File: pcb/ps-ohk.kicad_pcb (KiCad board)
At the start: 2 copper layers, 27 parts

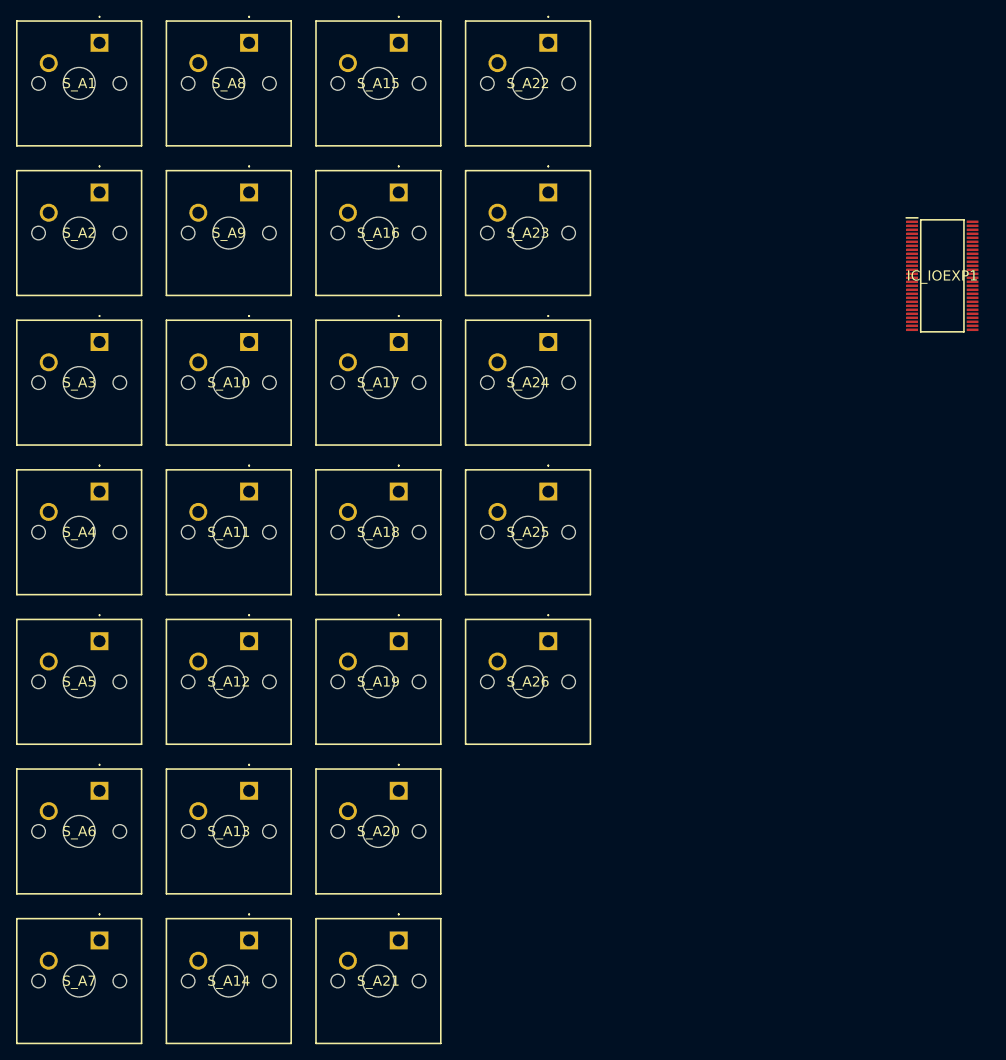
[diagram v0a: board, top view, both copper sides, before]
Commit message: pcb: implement IO Expander circuit based on proto
Signed-off-by: Dylan Turner <dylan.turner@tutanota.com>
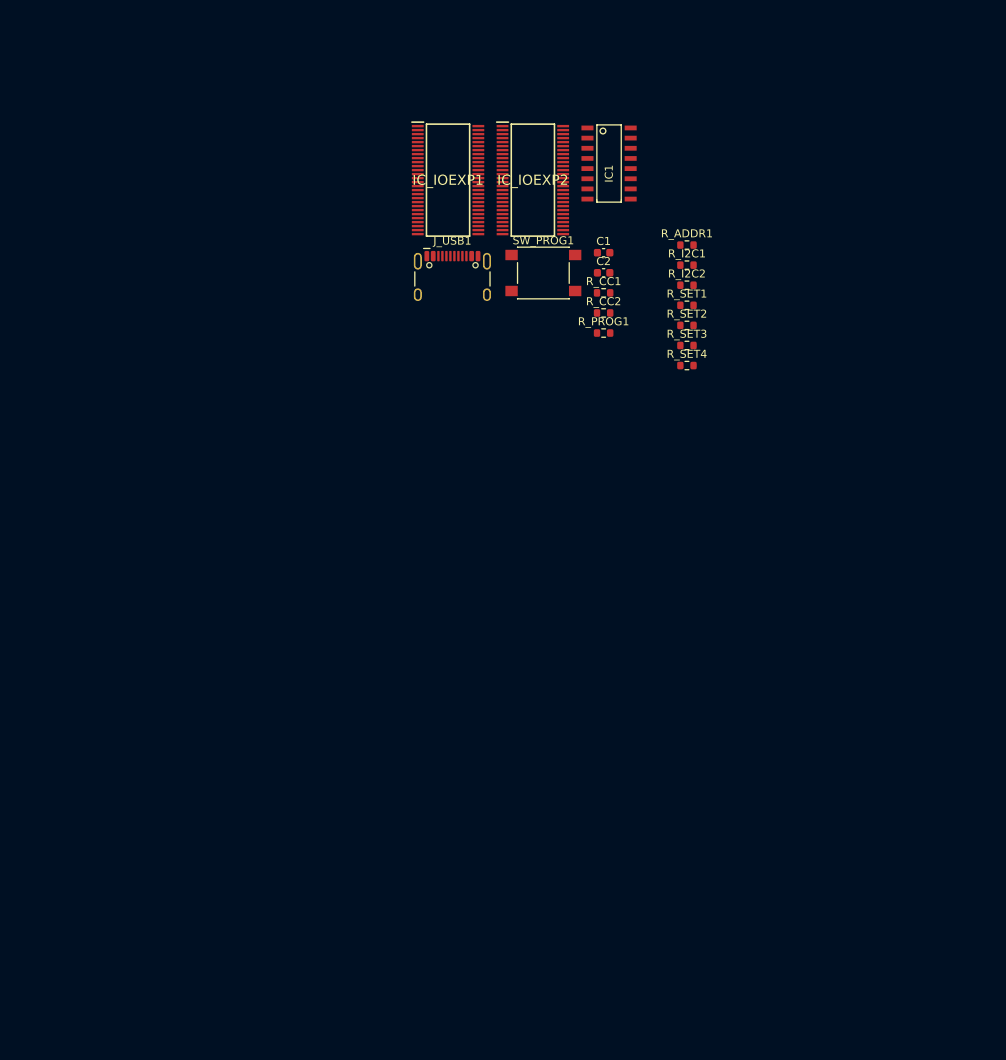
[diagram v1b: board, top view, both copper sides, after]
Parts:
- removed S_A1, S_A10, S_A11, S_A12, S_A13, S_A14, S_A15, S_A16, S_A17, S_A18, S_A19, S_A2, S_A20, S_A21, S_A22, S_A23, S_A24, S_A25, S_A26, S_A3, S_A4, S_A5, S_A6, S_A7, S_A8, S_A9: ~, COM-13834:COM13834
- added C1: 100nF, Capacitor_SMD:C_0603_1608Metric, F.Cu at (122.9, 78.9)
- added C2: 100nF, Capacitor_SMD:C_0603_1608Metric, F.Cu at (122.9, 81.4)
- added IC1: CH552G, ch552g:SOIC-16_3.9x9.9mm_Pitch1.27mm, F.Cu at (123.6, 67.7)
- added IC_IOEXP2: PCA9505DGGY, PCA9505DGGY:SOP50P810X120-56N, F.Cu at (114.0, 69.8)
- added J_USB1: ~, Connector_USB:USB_C_Receptacle_HCTL_HC-TYPE-C-16P-01A, F.Cu at (104.0, 83.0)
- added R_ADDR1: 1-10k, Resistor_SMD:R_0603_1608Metric, F.Cu at (133.3, 77.9)
- added R_CC1: 5.1k, Resistor_SMD:R_0603_1608Metric, F.Cu at (122.9, 83.9)
- added R_CC2: 5.1k, Resistor_SMD:R_0603_1608Metric, F.Cu at (122.9, 86.4)
- added R_I2C1: 1-10k, Resistor_SMD:R_0603_1608Metric, F.Cu at (133.3, 80.4)
- added R_I2C2: 1-10k, Resistor_SMD:R_0603_1608Metric, F.Cu at (133.3, 82.9)
- added R_PROG1: 10k, Resistor_SMD:R_0603_1608Metric, F.Cu at (122.9, 88.9)
- added R_SET1: 1-10k, Resistor_SMD:R_0603_1608Metric, F.Cu at (133.3, 85.4)
- added R_SET2: 1-10k, Resistor_SMD:R_0603_1608Metric, F.Cu at (133.3, 87.9)
- added R_SET3: 1-10k, Resistor_SMD:R_0603_1608Metric, F.Cu at (133.3, 90.5)
- added R_SET4: 1-10k, Resistor_SMD:R_0603_1608Metric, F.Cu at (133.3, 93.0)
- added SW_PROG1: ~, Button_Switch_SMD:SW_Push_1P1T_NO_6x6mm_H9.5mm, F.Cu at (115.3, 81.4)
- moved IC_IOEXP1 62.9 mm to (103.4, 69.8)
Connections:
- IC_IOEXP1 pad 1: unconnected-(IC_IOEXP1-SDA-Pad1) -> /SDA
- IC_IOEXP1 pad 11: unconnected-(IC_IOEXP1-VSS_2-Pad11) -> GND
- IC_IOEXP1 pad 18: unconnected-(IC_IOEXP1-VDD_1-Pad18) -> VCC
- IC_IOEXP1 pad 2: unconnected-(IC_IOEXP1-SCL-Pad2) -> /SCL
- IC_IOEXP1 pad 23: unconnected-(IC_IOEXP1-VSS_3-Pad23) -> GND
- IC_IOEXP1 pad 27: unconnected-(IC_IOEXP1-A0-Pad27) -> GND
- IC_IOEXP1 pad 28: unconnected-(IC_IOEXP1-A1-Pad28) -> GND
- IC_IOEXP1 pad 29: unconnected-(IC_IOEXP1-A2-Pad29) -> GND
- IC_IOEXP1 pad 3: unconnected-(IC_IOEXP1-IO0_0-Pad3) -> /KEY_A
- IC_IOEXP1 pad 30: unconnected-(IC_IOEXP1-~{OE}-Pad30) -> GND
- IC_IOEXP1 pad 34: unconnected-(IC_IOEXP1-VSS_4-Pad34) -> GND
- IC_IOEXP1 pad 39: unconnected-(IC_IOEXP1-VSS_5-Pad39) -> GND
- IC_IOEXP1 pad 46: unconnected-(IC_IOEXP1-VDD_2-Pad46) -> VCC
- IC_IOEXP1 pad 51: unconnected-(IC_IOEXP1-VSS_6-Pad51) -> GND
- IC_IOEXP1 pad 55: unconnected-(IC_IOEXP1-~{INT}-Pad55) -> Net-(IC_IOEXP1-~{INT})
- IC_IOEXP1 pad 56: unconnected-(IC_IOEXP1-~{RESET}-Pad56) -> Net-(IC_IOEXP1-~{RESET})
- IC_IOEXP1 pad 6: unconnected-(IC_IOEXP1-VSS_1-Pad6) -> GND

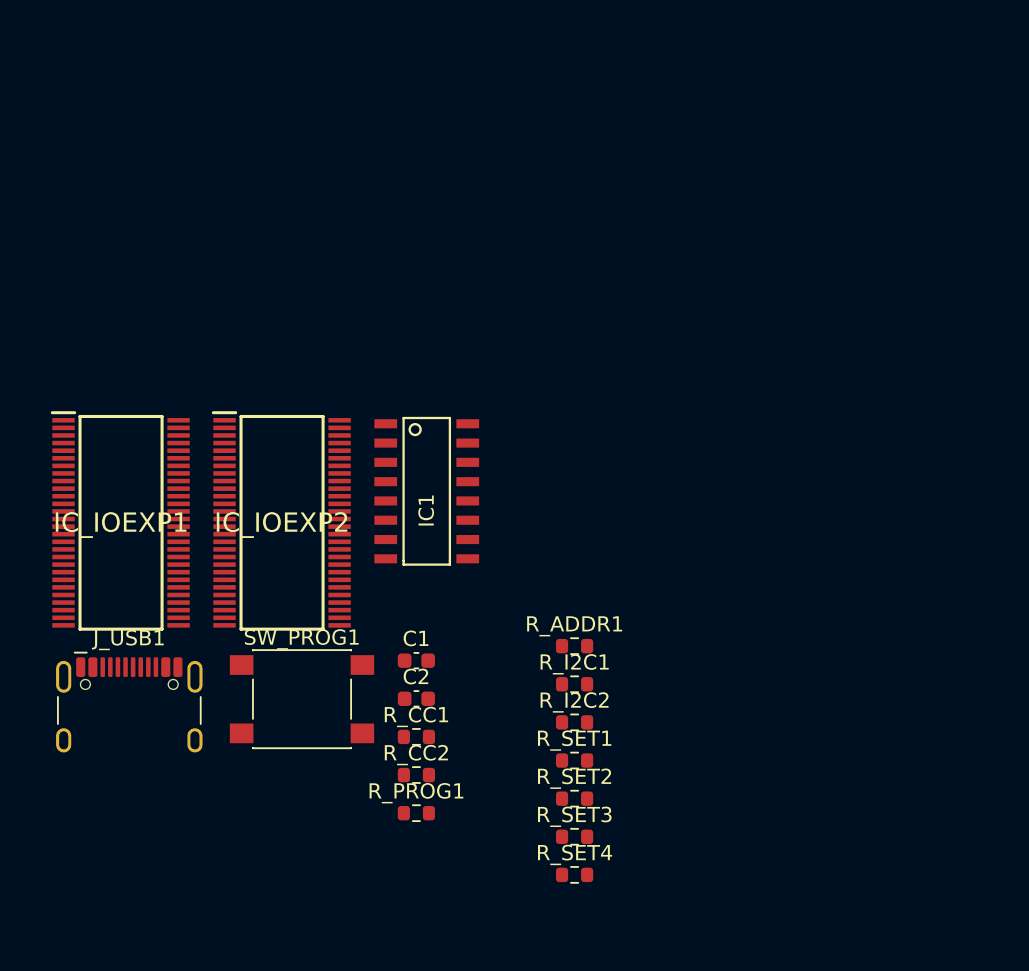
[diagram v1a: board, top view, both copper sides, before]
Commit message: pcb: moved libraries into pcb folder for org.
Signed-off-by: Dylan Turner <dylan.turner@tutanota.com>
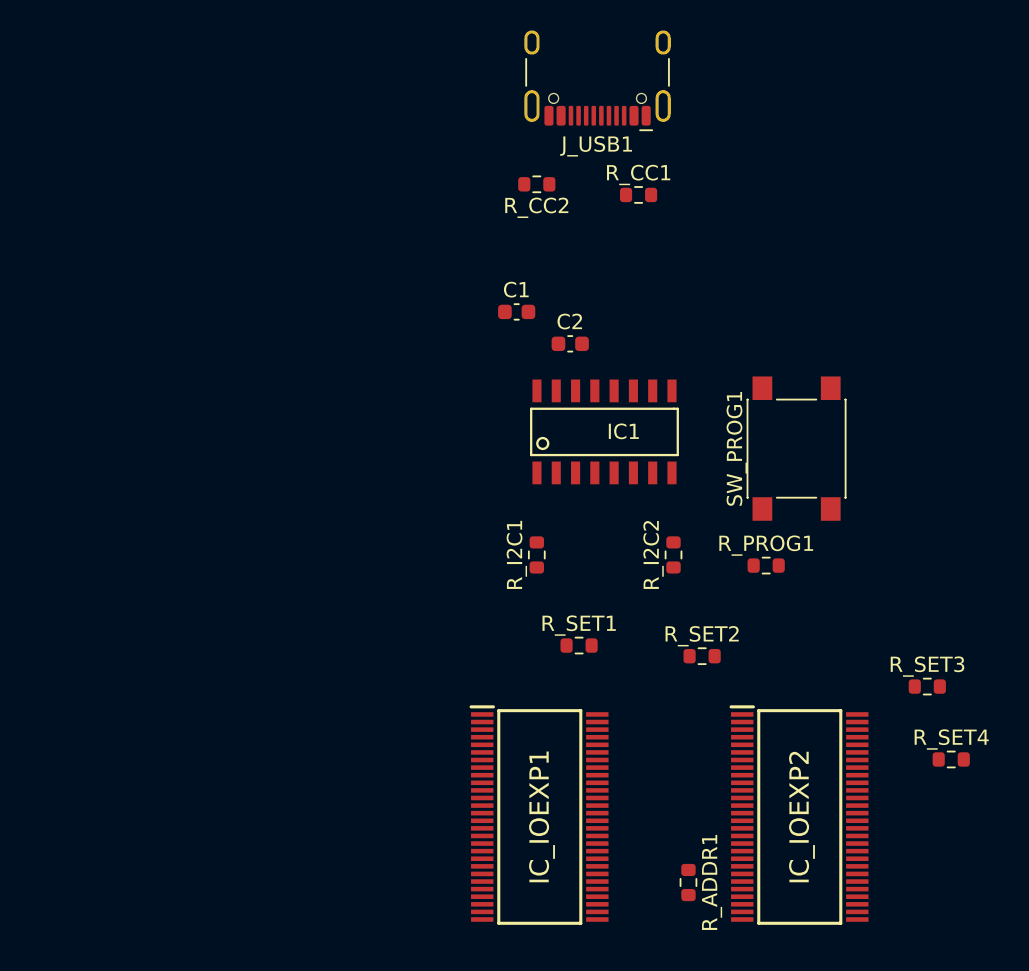
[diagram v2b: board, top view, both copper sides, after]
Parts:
- moved J_USB1 53.6 mm to (134.8, 39.2), turned to 180 degrees
- moved R_CC2 39.7 mm to (130.8, 47.5), turned to 180 degrees
- moved IC_IOEXP2 39.2 mm to (148.1, 89.2)
- moved R_CC1 38.6 mm to (137.5, 48.2)
- moved SW_PROG1 36.5 mm to (147.9, 64.9), turned to 90 degrees
- moved IC_IOEXP1 33.7 mm to (131.0, 89.2)
- moved R_PROG1 28.2 mm to (145.9, 72.6)
- moved R_SET4 25.9 mm to (158.1, 85.4)
- moved C2 25.5 mm to (133.0, 58.0)
- moved R_SET3 25.2 mm to (156.5, 80.6)
- moved C1 23.9 mm to (129.5, 55.9)
- moved R_ADDR1 17.3 mm to (140.8, 93.5), turned to -90 degrees
- moved R_I2C2 12.8 mm to (139.8, 71.9), turned to 90 degrees
- moved R_SET2 12.6 mm to (141.7, 78.6)
- moved IC1 12.3 mm to (135.3, 63.8), turned to 90 degrees
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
